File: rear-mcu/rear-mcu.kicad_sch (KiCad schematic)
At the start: 63 parts, among them J10 BSPD, J11 CAN, J12 SW, J13 PWR, J14 PROG, J2 Brake, J3 Current, J4 SDC, J5 Conn_02x10_Counter_Clockwise, J6 SDC, J7 SDC, J8 BSPD, J9 BSPD, SW1 SW_SPST, U1 STM32F103C8Tx, U2 SN65HVD256D, U3 AP2204K-ADJ, U4 AP2204K-ADJ, Y1 8M, Y2 32.768k

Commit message: change J5 connector
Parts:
- removed J10, J8, J9: BSPD, Connector_JST:JST_XH_B3B-XH-A_1x03_P2.50mm_Vertical, symbol Connector_Generic:Conn_01x03
- removed J11: CAN, Connector_JST:JST_XH_B3B-XH-A_1x03_P2.50mm_Vertical, symbol Connector_Generic:Conn_01x03
- removed J12: SW, Connector_JST:JST_XH_B3B-XH-A_1x03_P2.50mm_Vertical, symbol Connector_Generic:Conn_01x03
- removed J13: PWR, Connector_JST:JST_XH_B2B-XH-A_1x02_P2.50mm_Vertical, symbol Connector_Generic:Conn_01x02
- removed J14: PROG, Connector_PinHeader_2.54mm:PinHeader_1x03_P2.54mm_Vertical, symbol Connector_Generic:Conn_01x03
- removed J2: Brake, Connector_JST:JST_XH_B3B-XH-A_1x03_P2.50mm_Vertical, symbol Connector_Generic:Conn_01x03
- removed J3: Current, Connector_JST:JST_XH_B3B-XH-A_1x03_P2.50mm_Vertical, symbol Connector_Generic:Conn_01x03
- removed J4, J6, J7: SDC, Connector_JST:JST_XH_B3B-XH-A_1x03_P2.50mm_Vertical, symbol Connector_Generic:Conn_01x03
- removed J5: Conn_02x10_Counter_Clockwise, Connector_PinHeader_2.54mm:PinHeader_2x10_P2.54mm_Vertical, symbol Connector_Generic:Conn_02x10_Counter_Clockwise
- added J1: Conn_02x10_Odd_Even, symbol Connector_Generic:Conn_02x10_Odd_Even
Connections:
- net BSPD_signal1: now also J1.16 (Pin_16)
- net BSPD_signal2: now also J1.18 (Pin_18)
- net BSPD_signal3: now also J1.20 (Pin_20)
- net Brake_signal: now also J1.7 (Pin_7)
- net CAN+: now also J1.4 (Pin_4)
- net CAN-: now also J1.6 (Pin_6)
- net Current_signal: now also J1.9 (Pin_9)
- net GND: now also J1.15 (Pin_15), J1.17 (Pin_17), J1.19 (Pin_19)
- net SDC_signal1: now also J1.10 (Pin_10)
- net SDC_signal2: now also J1.12 (Pin_12)
- net SDC_signal3: now also J1.14 (Pin_14)
- net SWDCLK: now also J1.13 (Pin_13)
- net SWDIO: now also J1.11 (Pin_11)
- net SW_signal: now also J1.2 (Pin_2)
- net VDC: now also J1.1 (Pin_1), J1.3 (Pin_3), J1.5 (Pin_5)
- no-connect marks 22 -> 21
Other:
- note removed: "SWD"
- moved on the sheet: C16, R22, R23, U2

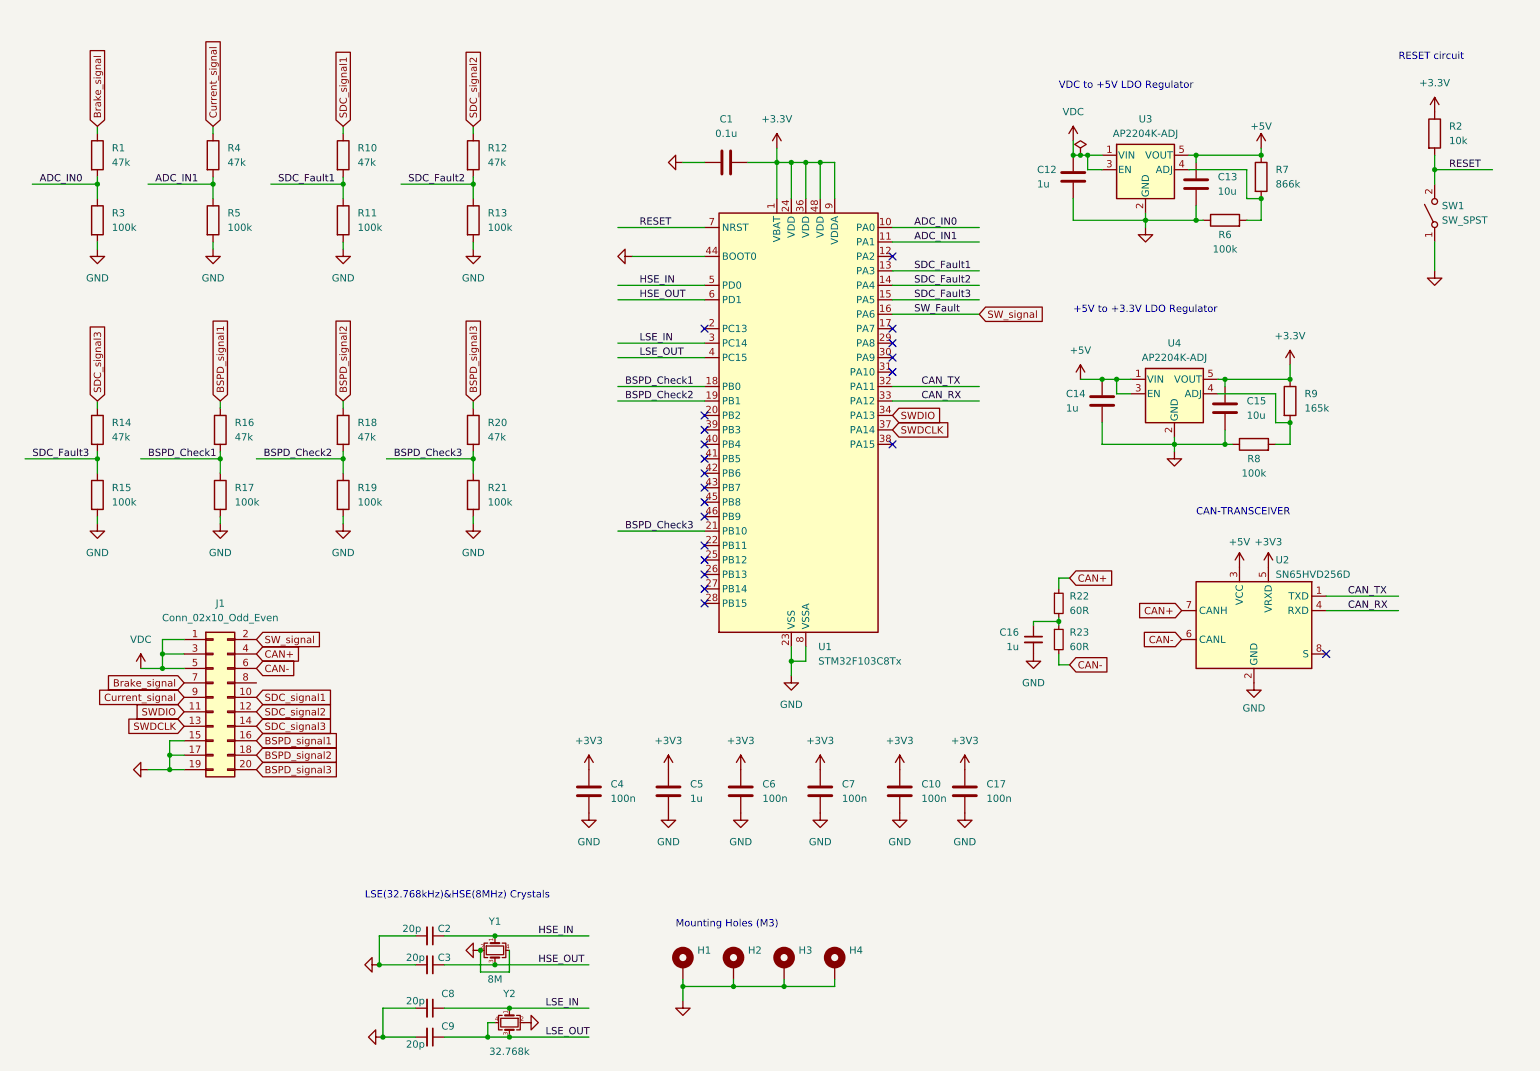
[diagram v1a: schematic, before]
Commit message: add USB connector and modify footprints
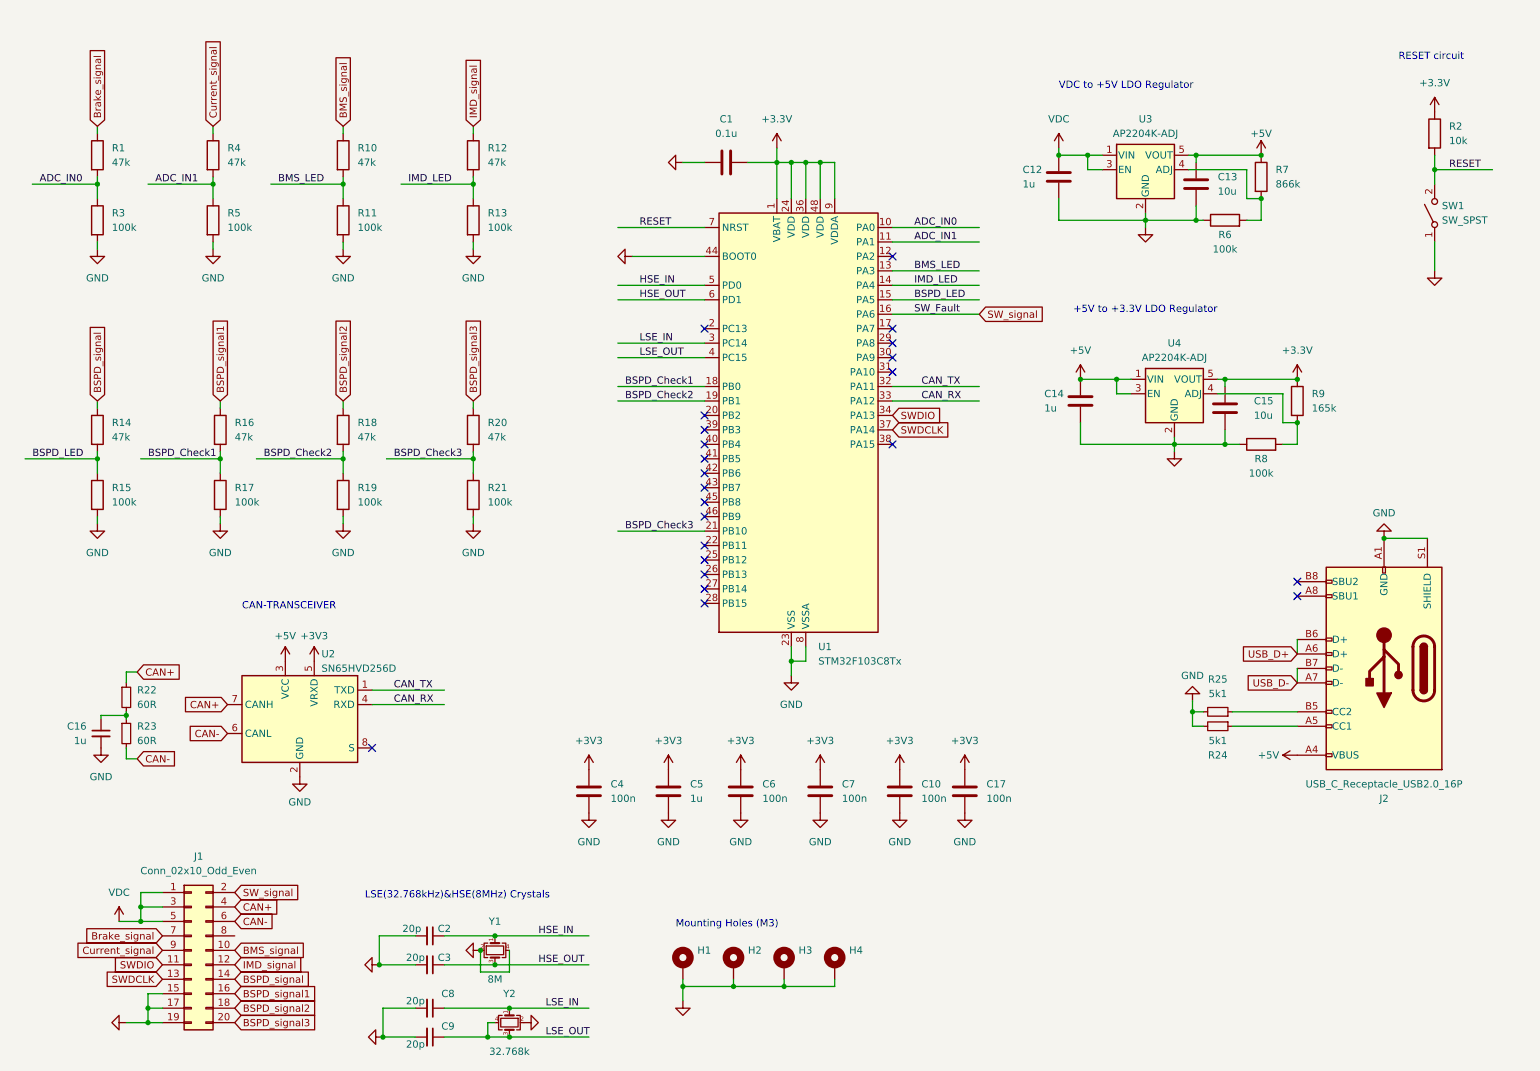
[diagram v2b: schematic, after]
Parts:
- added J2: USB_C_Receptacle_USB2.0_16P, Connector_USB:USB_C_Receptacle_HRO_TYPE-C-31-M-12, symbol Connector:USB_C_Receptacle_USB2.0_16P
- added R24, R25: 5k1, Resistor_SMD:R_0603_1608Metric, symbol Device:R_Small
- C1: footprint (none) -> Capacitor_SMD:C_0603_1608Metric
- C10, C17, C4, C5, C6, C7: footprint Resistor_SMD:R_0603_1608Metric -> Capacitor_SMD:C_0603_1608Metric
- C12, C14: footprint Capacitor_SMD:C_0805_2012Metric -> Capacitor_SMD:C_0603_1608Metric
- H1, H2, H3, H4: footprint MountingHole:MountingHole_2.2mm_M2_Pad -> MountingHole:MountingHole_3.2mm_M3_ISO14580_Pad
- J1: footprint (none) -> Connector_PinHeader_2.54mm:PinHeader_2x10_P2.54mm_Vertical
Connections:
- net +5V: now also J2.A4 (VBUS), J2.A9 (VBUS), J2.B4 (VBUS), J2.B9 (VBUS)
- net GND: now also J2.A1 (GND), J2.A12 (GND), J2.B1 (GND), J2.B12 (GND), J2.S1 (SHIELD), R24.2, R25.2
- net SDC_Fault1 renamed BMS_LED
- net SDC_Fault2 renamed IMD_LED
- net SDC_Fault3 renamed BSPD_LED
- net SDC_signal1 renamed BMS_signal
- net SDC_signal2 renamed IMD_signal
- net SDC_signal3 renamed BSPD_signal
- new net: J2.A5 (CC1), R24.1
- new net: J2.B5 (CC2), R25.1
- new net USB_D+: J2.A6 (D+), J2.B6 (D+)
- new net USB_D-: J2.A7 (D-), J2.B7 (D-)
- no-connect marks 21 -> 23
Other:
- moved on the sheet: C12, C14, C16, J1, R22, R23, R8, R9, U2

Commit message: layout
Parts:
- removed C1: 0.1u, Capacitor_SMD:C_0603_1608Metric, symbol Device:C
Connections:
- net +3V3 is gone; now on net +3.3V: C10.1, C17.1, C4.1, C5.1, C6.1, C7.1, U2.5 (VRXD)
- net BMS_signal: now also J1.4 (Pin_4); no longer J1.10 (Pin_10)
- net BSPD_signal: now also J1.8 (Pin_8); no longer J1.14 (Pin_14)
- net BSPD_signal1: now also J1.10 (Pin_10); no longer J1.16 (Pin_16)
- net BSPD_signal2: now also J1.12 (Pin_12); no longer J1.18 (Pin_18)
- net BSPD_signal3: now also J1.14 (Pin_14); no longer J1.20 (Pin_20)
- net CAN+: now also J1.20 (Pin_20); no longer J1.4 (Pin_4)
- net CAN-: now also J1.18 (Pin_18); no longer J1.6 (Pin_6)
- net CAN_RX: now also U1.46 (PB9); no longer U1.33 (PA12)
- net CAN_TX: now also U1.45 (PB8); no longer U1.32 (PA11)
- net IMD_signal: now also J1.6 (Pin_6); no longer J1.12 (Pin_12)
- net SWDCLK: now also J1.11 (Pin_11); no longer J1.13 (Pin_13)
- net SWDIO: now also J1.13 (Pin_13); no longer J1.11 (Pin_11)
- net USB_D+: now also U1.33 (PA12)
- net USB_D-: now also U1.32 (PA11)
- no-connect marks 23 -> 21

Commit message: layout
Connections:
- net BMS_LED: now also U1.21 (PB10); no longer U1.13 (PA3)
- net BSPD_Check1: now also U1.16 (PA6); no longer U1.18 (PB0)
- net BSPD_Check2: now also U1.15 (PA5); no longer U1.19 (PB1)
- net BSPD_Check3: now also U1.14 (PA4); no longer U1.21 (PB10)
- net BSPD_LED: now also U1.18 (PB0); no longer U1.15 (PA5)
- net IMD_LED: now also U1.19 (PB1); no longer U1.14 (PA4)
- net SW_signal: now also U1.13 (PA3); no longer U1.16 (PA6)

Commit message: finish layout
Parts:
- added C1, C11: 100n, Capacitor_SMD:C_0603_1608Metric, symbol Device:C
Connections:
- net +3.3V: now also C1.1
- net +5V: now also C11.1
- net GND: now also C1.2, C11.2
- net Brake_signal renamed Brake_signal1
- net Current_signal renamed Brake_signal2
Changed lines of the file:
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@@
     (effects (font (size 1.27 1.27)) (justify left bottom))
-  )
-  (global_label "Current_signal" (shape input) (at 49.53 30.48 90) (fields_autoplaced)
-    (effects (font (size 1.27 1.27)) (justify left))
-    (property "Intersheetrefs" "${INTERSHEET_REFS}" (at 49.53 13.8274 90)
-      (effects (font (size 1.27 1.27)) (justify left) hide)
-    )
   )
   (global_label "CAN+" (shape input) (at 36.195 126.365 0) (fields_autoplaced)
@@
     )
   )
-  (global_label "Brake_signal" (shape input) (at 40.64 172.72 180) (fields_autoplaced)
+  (global_label "Brake_signal1" (shape input) (at 40.64 172.72 180) (fields_autoplaced)
     (effects (font (size 1.27 1.27)) (justify right))
-    (property "Intersheetrefs" "${INTERSHEET_REFS}" (at 25.6202 172.72 0)
+    (property "Intersheetrefs" "${INTERSHEET_REFS}" (at 24.4107 172.72 0)
       (effects (font (size 1.27 1.27)) (justify right) hide)
     )
@@
     (property "Intersheetrefs" "${INTERSHEET_REFS}" (at 69.2669 180.34 0)
       (effects (font (size 1.27 1.27)) (justify left) hide)
+    )
+  )
+  (global_label "Brake_signal2" (shape input) (at 40.64 175.26 180) (fields_autoplaced)
+    (effects (font (size 1.27 1.27)) (justify right))
+    (property "Intersheetrefs" "${INTERSHEET_REFS}" (at 24.4107 175.26 0)
+      (effects (font (size 1.27 1.27)) (justify right) hide)
     )
   )
@@
     )
   )
+  (global_label "Brake_signal2" (shape input) (at 49.53 30.48 90) (fields_autoplaced)
+    (effects (font (size 1.27 1.27)) (justify left))
+    (property "Intersheetrefs" "${INTERSHEET_REFS}" (at 49.53 14.2507 90)
+      (effects (font (size 1.27 1.27)) (justify left) hide)
+    )
+  )
   (global_label "SWDCLK" (shape input) (at 40.64 177.8 180) (fields_autoplaced)
     (effects (font (size 1.27 1.27)) (justify right))
@@
     )
   )
-  (global_label "Brake_signal" (shape input) (at 29.21 30.48 90) (fields_autoplaced)
-    (effects (font (size 1.27 1.27)) (justify left))
-    (property "Intersheetrefs" "${INTERSHEET_REFS}" (at 29.21 15.4602 90)
+  (global_label "Brake_signal1" (shape input) (at 29.21 30.48 90) (fields_autoplaced)
+    (effects (font (size 1.27 1.27)) (justify left))
+    (property "Intersheetrefs" "${INTERSHEET_REFS}" (at 29.21 14.2507 90)
       (effects (font (size 1.27 1.27)) (justify left) hide)
     )
@@
     (property "Intersheetrefs" "${INTERSHEET_REFS}" (at 66.9688 167.64 0)
       (effects (font (size 1.27 1.27)) (justify left) hide)
-    )
-  )
-  (global_label "Current_signal" (shape input) (at 40.64 175.26 180) (fields_autoplaced)
-    (effects (font (size 1.27 1.27)) (justify right))
-    (property "Intersheetrefs" "${INTERSHEET_REFS}" (at 23.9874 175.26 0)
-      (effects (font (size 1.27 1.27)) (justify right) hide)
     )
   )
@@
     )
   )
+  (symbol (lib_id "power:+3.3V") (at 17.78 114.3 0) (unit 1)
+    (in_bom yes) (on_board yes) (dnp no) (fields_autoplaced)
+    (property "Reference" "#PWR035" (at 17.78 118.11 0)
+      (effects (font (size 1.27 1.27)) hide)
+    )
+    (property "Value" "+3.3V" (at 17.78 109.22 0)
+      (effects (font (size 1.27 1.27)))
+    )
+    (property "Footprint" "" (at 17.78 114.3 0)
+      (effects (font (size 1.27 1.27)) hide)
+    )
+    (property "Datasheet" "" (at 17.78 114.3 0)
+      (effects (font (size 1.27 1.27)) hide)
+    )
+    (pin "1")
+    (instances
+      (project "rear-mcu"
+        (path "/df5b5f24-3d61-486a-be7e-cedc462763e6"
+          (reference "#PWR035") (unit 1)
+        )
+      )
+    )
+  )
   (symbol (lib_id "Device:C") (at 227.33 80.01 0) (unit 1)
     (in_bom yes) (on_board yes) (dnp no)
@@
     )
   )
+  (symbol (lib_id "power:GND") (at 16.51 147.32 0) (unit 1)
+    (in_bom yes) (on_board yes) (dnp no)
+    (property "Reference" "#PWR041" (at 16.51 153.67 0)
+      (effects (font (size 1.27 1.27)) hide)
+    )
+    (property "Value" "GND" (at 16.51 152.4 0)
+      (effects (font (size 1.27 1.27)))
+    )
+    (property "Footprint" "" (at 16.51 147.32 0)
+      (effects (font (size 1.27 1.27)) hide)
+    )
+    (property "Datasheet" "" (at 16.51 147.32 0)
+      (effects (font (size 1.27 1.27)) hide)
+    )
+    (pin "1")
+    (instances
+      (project "rear-mcu"
+        (path "/df5b5f24-3d61-486a-be7e-cedc462763e6"
+          (reference "#PWR041") (unit 1)
+        )
+      )
+    )
+  )
   (symbol (lib_id "power:+5V") (at 201.93 74.93 0) (unit 1)
     (in_bom yes) (on_board yes) (dnp no) (fields_autoplaced)
@@
         (path "/df5b5f24-3d61-486a-be7e-cedc462763e6"
           (reference "#PWR062") (unit 1)
+        )
+      )
+    )
+  )
+  (symbol (lib_id "Device:C") (at 17.78 118.11 0) (unit 1)
+    (in_bom yes) (on_board yes) (dnp no) (fields_autoplaced)
+    (property "Reference" "C1" (at 21.59 116.84 0)
+      (effects (font (size 1.27 1.27)) (justify left))
+    )
+    (property "Value" "100n" (at 21.59 119.38 0)
+      (effects (font (size 1.27 1.27)) (justify left))
+    )
+    (property "Footprint" "Capacitor_SMD:C_0603_1608Metric" (at 18.7452 121.92 0)
+      (effects (font (size 1.27 1.27)) hide)
+    )
+    (property "Datasheet" "~" (at 17.78 118.11 0)
+      (effects (font (size 1.27 1.27)) hide)
+    )
+    (pin "1")
+    (pin "2")
+    (instances
+      (project "rear-mcu"
+        (path "/df5b5f24-3d61-486a-be7e-cedc462763e6"
+          (reference "C1") (unit 1)
         )
       )
@@
     )
   )
+  (symbol (lib_id "Device:C") (at 16.51 143.51 0) (unit 1)
+    (in_bom yes) (on_board yes) (dnp no) (fields_autoplaced)
+    (property "Reference" "C11" (at 20.32 142.24 0)
+      (effects (font (size 1.27 1.27)) (justify left))
+    )
+    (property "Value" "100n" (at 20.32 144.78 0)
+      (effects (font (size 1.27 1.27)) (justify left))
+    )
+    (property "Footprint" "Capacitor_SMD:C_0603_1608Metric" (at 17.4752 147.32 0)
+      (effects (font (size 1.27 1.27)) hide)
+    )
+    (property "Datasheet" "~" (at 16.51 143.51 0)
+      (effects (font (size 1.27 1.27)) hide)
+    )
+    (pin "1")
+    (pin "2")
+    (instances
+      (project "rear-mcu"
+        (path "/df5b5f24-3d61-486a-be7e-cedc462763e6"
+          (reference "C11") (unit 1)
+        )
+      )
+    )
+  )
   (symbol (lib_id "power:+3.3V") (at 181.61 143.51 0) (unit 1)
     (in_bom yes) (on_board yes) (dnp no) (fields_autoplaced)
@@
         (path "/df5b5f24-3d61-486a-be7e-cedc462763e6"
           (reference "#PWR018") (unit 1)
+        )
+      )
+    )
+  )
+  (symbol (lib_id "power:+5V") (at 16.51 139.7 0) (unit 1)
+    (in_bom yes) (on_board yes) (dnp no) (fields_autoplaced)
+    (property "Reference" "#PWR039" (at 16.51 143.51 0)
+      (effects (font (size 1.27 1.27)) hide)
+    )
+    (property "Value" "+5V" (at 16.51 135.255 0)
+      (effects (font (size 1.27 1.27)))
+    )
+    (property "Footprint" "" (at 16.51 139.7 0)
+      (effects (font (size 1.27 1.27)) hide)
+    )
+    (property "Datasheet" "" (at 16.51 139.7 0)
+      (effects (font (size 1.27 1.27)) hide)
+    )
+    (pin "1")
+    (instances
+      (project "rear-mcu"
+        (path "/df5b5f24-3d61-486a-be7e-cedc462763e6"
+          (reference "#PWR039") (unit 1)
         )
       )
@@
         )
       )
+    )
+  )
+  (symbol (lib_id "power:GND") (at 17.78 121.92 0) (unit 1)
+    (in_bom yes) (on_board yes) (dnp no)
+    (property "Reference" "#PWR037" (at 17.78 128.27 0)
+      (effects (font (size 1.27 1.27)) hide)
+    )
+    (property "Value" "GND" (at 17.78 127 0)
+      (effects (font (size 1.27 1.27)))
+    )
+    (property "Footprint" "" (at 17.78 121.92 0)
+      (effects (font (size 1.27 1.27)) hide)
+    )
+    (property "Datasheet" "" (at 17.78 121.92 0)
+      (effects (font (size 1.27 1.27)) hide)
+    )
+    (pin "1")
+    (instances
+      (project "rear-mcu"
+        (path "/df5b5f24-3d61-486a-be7e-cedc462763e6"
+          (reference "#PWR037") (unit 1)
+        )
+      )
